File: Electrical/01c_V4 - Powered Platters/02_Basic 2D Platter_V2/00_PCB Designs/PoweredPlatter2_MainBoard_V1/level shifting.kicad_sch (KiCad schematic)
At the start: 4 parts, among them U2 74HC3G34DC

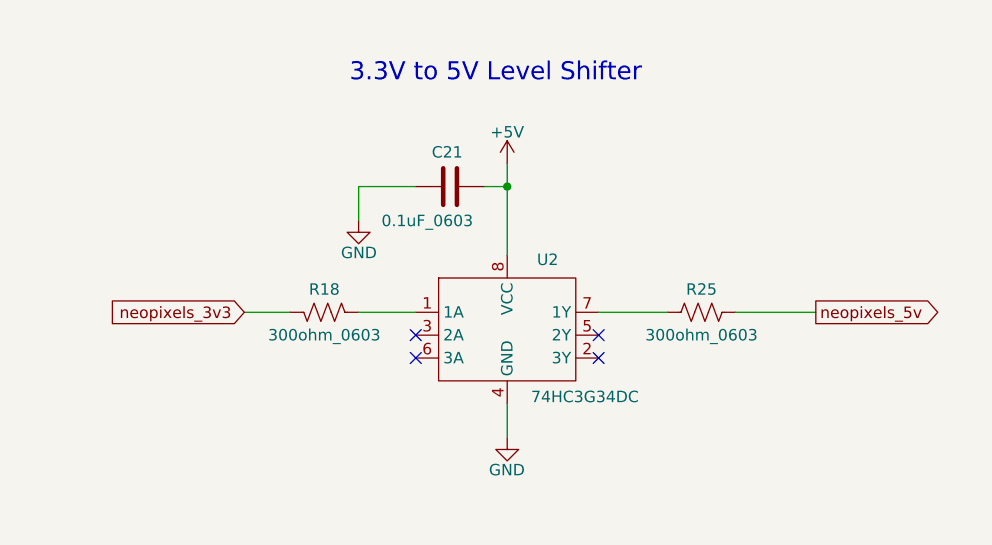
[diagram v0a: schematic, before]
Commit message: second powered platter main PCB designed and ready for CNC milling
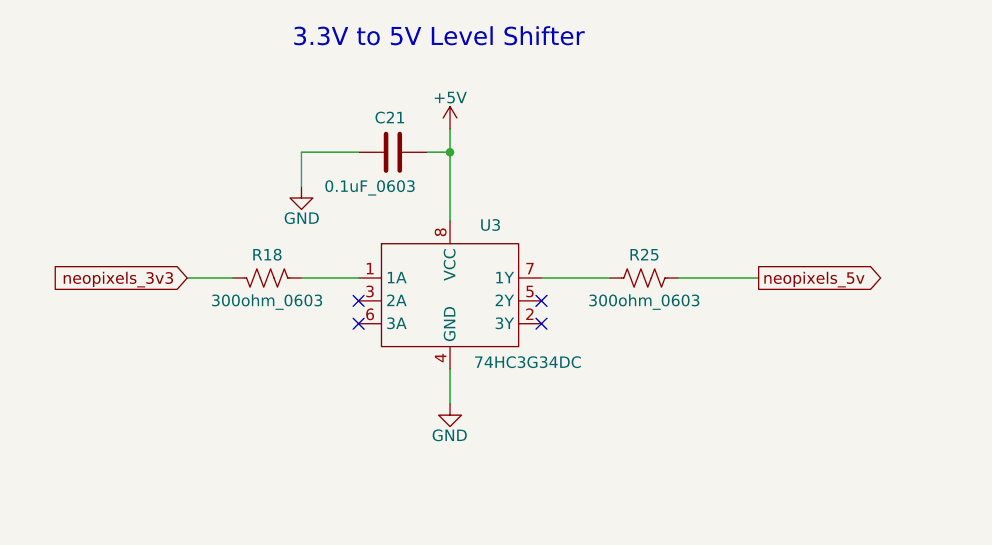
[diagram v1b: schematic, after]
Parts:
- removed U2: 74HC3G34DC, PixelPlatter:74HC3G34DC, symbol HDD_CLK_V6.0:74HC3G34DC
- added U3: 74HC3G34DC, PixelPlatter:74HC3G34DC, symbol HDD_CLK_V6.0:74HC3G34DC
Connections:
- net +5V: now also U3.8 (VCC)
- net GND: now also U3.4 (GND)
- net at R18.1: now also U3.1 (1A)
- net at R25.2: now also U3.7 (1Y)

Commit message: small updates - pushing to move to other computer
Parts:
- C21, R18, R25, U3: now not fitted
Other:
- note added: "Populate later if Neopixels are ran Saving the effort for now"
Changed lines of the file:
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@@
+		)
+	)
+	(text "Populate later if Neopixels are ran\nSaving the effort for now"
+		(exclude_from_sim no)
+		(at 113.03 124.714 0)
+		(effects
+			(font
+				(size 2 2)
+				(thickness 0.25)
+				(color 255 45 76 1)
+			)
+			(justify left bottom)
 		)
 	)
@@
 		(on_board yes)
 		(in_pos_files yes)
-		(dnp no)
+		(dnp yes)
 		(property "Reference" "C21"
 			(at 135.128 80.01 90)
@@
 		(on_board yes)
 		(in_pos_files yes)
-		(dnp no)
+		(dnp yes)
 		(property "Reference" "U3"
 			(at 146.812 91.948 0)
@@
 		(on_board yes)
 		(in_pos_files yes)
-		(dnp no)
+		(dnp yes)
 		(property "Reference" "R18"
 			(at 123.19 95.25 90)
@@
 		(on_board yes)
 		(in_pos_files yes)
-		(dnp no)
+		(dnp yes)
 		(property "Reference" "R25"
 			(at 165.1 95.25 90)
